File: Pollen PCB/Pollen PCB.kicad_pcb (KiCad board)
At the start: 2 copper layers, 3 parts, among them U1 DS18B20, U2 Pico

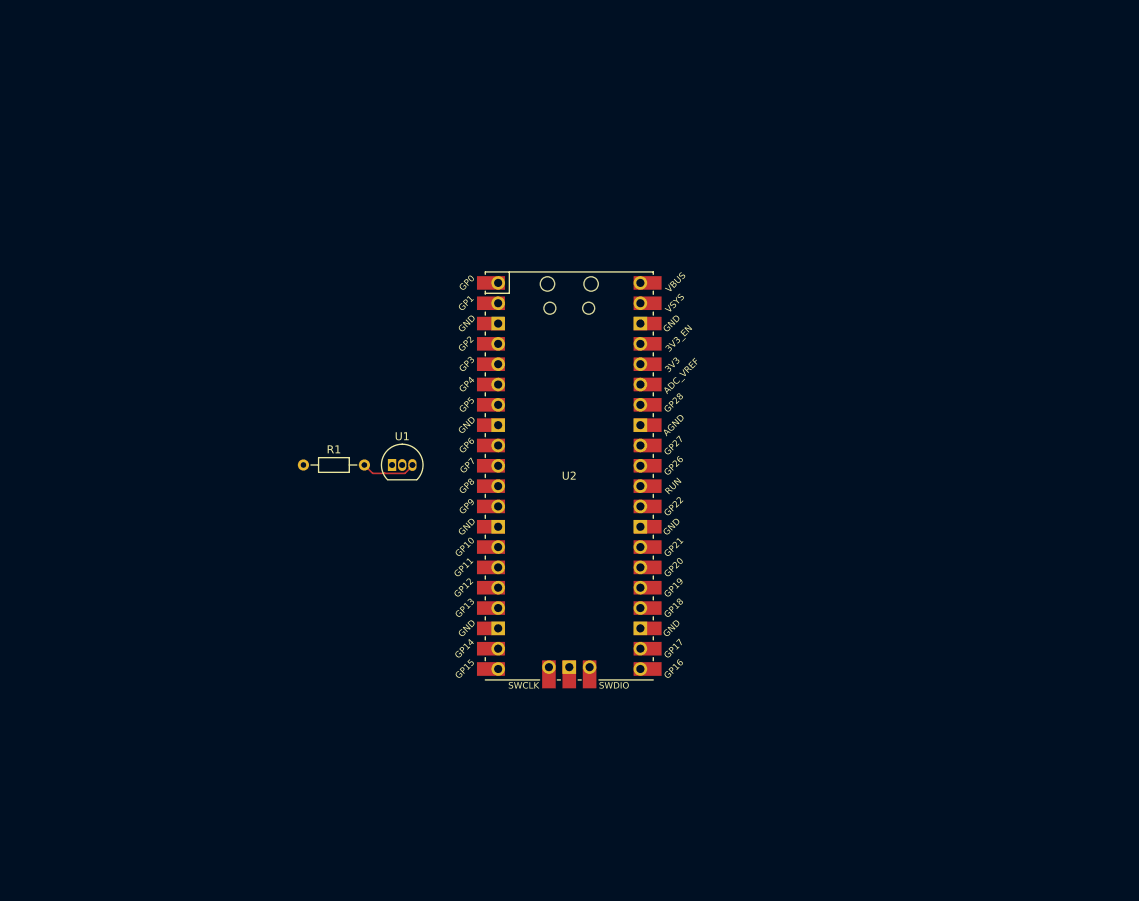
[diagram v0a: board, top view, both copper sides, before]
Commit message: Start drawing the schematic
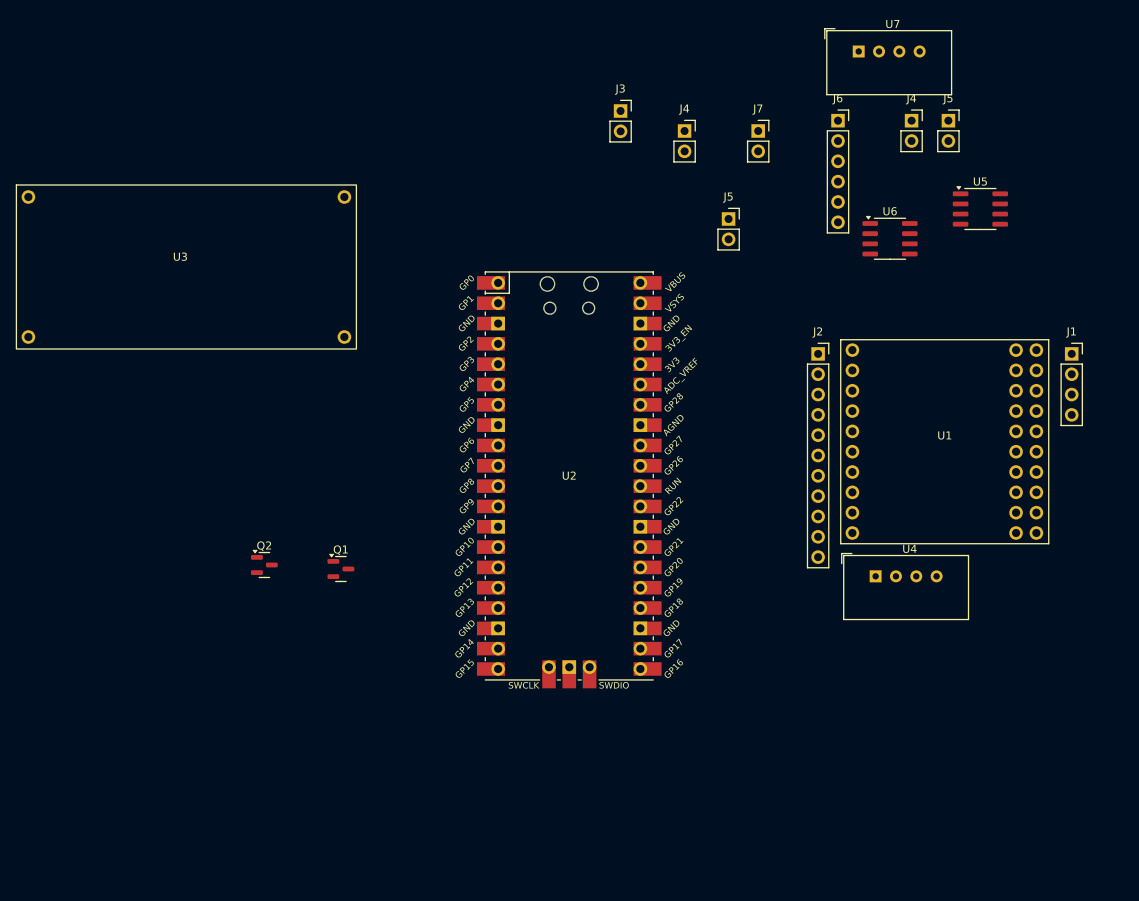
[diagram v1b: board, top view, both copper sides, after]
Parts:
- removed R1: R, Resistor_THT:R_Axial_DIN0204_L3.6mm_D1.6mm_P7.62mm_Horizontal
- added J1: GY-GPS6MV2, Connector_PinSocket_2.54mm:PinSocket_1x04_P2.54mm_Vertical, F.Cu at (228.4, 80.1)
- added J2: Conn_01x11_Socket, Connector_PinSocket_2.54mm:PinSocket_1x11_P2.54mm_Vertical, F.Cu at (196.7, 80.1)
- added J3: Solar_panel, Connector_PinSocket_2.54mm:PinSocket_1x02_P2.54mm_Vertical, F.Cu at (172.0, 49.8)
- added J4: Solar_panel, Connector_PinSocket_2.54mm:PinSocket_1x02_P2.54mm_Vertical, F.Cu at (180.0, 52.2)
- added J4: Solar_panel, Connector_PinSocket_2.54mm:PinSocket_1x02_P2.54mm_Vertical, F.Cu at (208.4, 51.0)
- added J5: Solar_charger, Connector_PinSocket_2.54mm:PinSocket_1x02_P2.54mm_Vertical, F.Cu at (185.5, 63.2)
- added J5: Solar_charger, Connector_PinSocket_2.54mm:PinSocket_1x02_P2.54mm_Vertical, F.Cu at (213.0, 51.0)
- added J6: Raspberry Pi, Connector_PinSocket_2.54mm:PinSocket_1x06_P2.54mm_Vertical, F.Cu at (199.2, 51.0)
- added J7: Battery, Connector_PinSocket_2.54mm:PinSocket_1x02_P2.54mm_Vertical, F.Cu at (189.2, 52.2)
- added Q1: Si2319CDS, Package_TO_SOT_SMD:SOT-23, F.Cu at (137.1, 107.0)
- added Q2: MMBT2222A, Package_TO_SOT_SMD:SOT-23, F.Cu at (127.5, 106.5)
- added U3: XL6009_DC-DC, Custom_Components:XL6009_DC-DC, F.Cu at (117.0, 68.5)
- added U4: DHT22, Sensor:ASAIR_AM2302_P2.54mm_Vertical, F.Cu at (203.9, 107.9)
- added U5: INA219AxD, Package_SO:SOIC-8_3.9x4.9mm_P1.27mm, F.Cu at (217.0, 62.0)
- added U6: INA219AxD, Package_SO:SOIC-8_3.9x4.9mm_P1.27mm, F.Cu at (205.7, 65.7)
- added U7: DHT22, Sensor:ASAIR_AM2302_P2.54mm_Vertical, F.Cu at (201.8, 42.3)
- U1: value DS18B20 -> NB-IOT-BC660; footprint Package_TO_SOT_THT:TO-92_Inline -> Custom_Components:NB-IOT-BC660
- moved U1 69.2 mm to (212.5, 90.8)
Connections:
- U1 pad 2: Net-(U1-DQ) -> unconnected-(U1-Pin_2-Pad2)
- U1 pad 3: Net-(U1-V_{DD}) -> unconnected-(U1-VCC-Pad3)
- U2 pad 4: unconnected-(U2-GPIO2-Pad4) -> Net-(U2-GPIO2)
- U2 pad 6: unconnected-(U2-GPIO4-Pad6) -> Net-(U2-GPIO4)
- U2 pad 7: unconnected-(U2-GPIO5-Pad7) -> Net-(U2-GPIO5)
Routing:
- net Net-(U1-V_{DD}): track 6.98 -> 0.00 mm

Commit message: Schematic v1.0
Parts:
- added C1: 100nF, Capacitor_THT:C_Axial_L5.1mm_D3.1mm_P10.00mm_Horizontal, F.Cu at (224.0, 116.5)
- added Q3: MMBT2222A, Package_TO_SOT_SMD:SOT-23, F.Cu at (129.6, 118.9)
- added Q4: Si2319CDS, Package_TO_SOT_SMD:SOT-23, F.Cu at (129.6, 123.5)
- J2: value Conn_01x11_Socket -> Adafruit Charge Controller
- moved U4 12.2 mm to (204.2, 120.1)
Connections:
- net BATT_CHG renamed /CHARGER_LIPO
- net BATT_V+ renamed /BATTERY+
- net Net-(U2-GPIO2) renamed /3V3_SENSOR_CONTROL
- net Net-(U2-GPIO4) renamed /SDA
- net Net-(U2-GPIO5) renamed /SCL
- net SOLAR_CHG renamed /CHARGER_V+
- net SOLAR_V+ renamed /SOLAR_V+
- J1 pad 1: unconnected-(J1-VCC-Pad1) -> +5V
- J1 pad 2: unconnected-(J1-RX-Pad2) -> /GPS_RX
- J1 pad 3: unconnected-(J1-TX-Pad3) -> /GPS_TX
- J1 pad 4: unconnected-(J1-GND-Pad4) -> GND
- J2 pad 11: unconnected-(J2-GND-Pad11) -> GND
- J2 pad 6: unconnected-(J2-PGOOD-Pad6) -> /CHARGER_PGOOD
- J2 pad 7: unconnected-(J2-CHG-Pad7) -> /CHARGER_CHG
- J2 pad 8: VCC -> +BATT
- J2 pad 9: unconnected-(J2-GND-Pad9) -> GND
- J6 pad 1: VCC_5V -> +5V
- J6 pad 3: unconnected-(J6-Pin_3-Pad3) -> /RPI_MOSI
- J6 pad 4: unconnected-(J6-Pin_4-Pad4) -> /RPI_MISO
- J6 pad 5: unconnected-(J6-Pin_5-Pad5) -> /RPI_SCK
- J6 pad 6: unconnected-(J6-Pin_6-Pad6) -> /RPI_CS
- Q1 pad 3: VCC -> +BATT
- U1 pad 19: unconnected-(U1-RxD-Pad19) -> /NB-IOT_RX
- U1 pad 20: unconnected-(U1-TxD-Pad20) -> /NB-IOT_TX
- U1 pad 3: unconnected-(U1-VCC-Pad3) -> +3V3
- U1 pad 4: unconnected-(U1-GND-Pad4) -> GND
- U1 pad 9: unconnected-(U1-RST-Pad9) -> /NB-IOT_RST
- U2 pad 1: unconnected-(U2-GPIO0-Pad1) -> /NB-IOT_RX
- U2 pad 11: unconnected-(U2-GPIO8-Pad11) -> /GPS_RX
- U2 pad 12: unconnected-(U2-GPIO9-Pad12) -> /GPS_TX
- U2 pad 13: unconnected-(U2-GND-Pad13) -> GND
- U2 pad 14: unconnected-(U2-GPIO10-Pad14) -> /CHARGER_CHG
- U2 pad 15: unconnected-(U2-GPIO11-Pad15) -> /CHARGER_PGOOD
- U2 pad 18: unconnected-(U2-GND-Pad18) -> GND
- U2 pad 19: unconnected-(U2-GPIO14-Pad19) -> /DHT_1
- U2 pad 2: unconnected-(U2-GPIO1-Pad2) -> /NB-IOT_TX
- U2 pad 20: unconnected-(U2-GPIO15-Pad20) -> /DHT_2
- U2 pad 21: unconnected-(U2-GPIO16-Pad21) -> /RPI_MISO
- U2 pad 22: unconnected-(U2-GPIO17-Pad22) -> /RPI_CS
- U2 pad 23: unconnected-(U2-GND-Pad23) -> GND
- U2 pad 24: unconnected-(U2-GPIO18-Pad24) -> /RPI_SCK
- U2 pad 25: unconnected-(U2-GPIO19-Pad25) -> /RPI_MOSI
- U2 pad 28: unconnected-(U2-GND-Pad28) -> GND
- U2 pad 3: unconnected-(U2-GND-Pad3) -> GND
- U2 pad 36: unconnected-(U2-3V3-Pad36) -> +3V3
- U2 pad 38: unconnected-(U2-GND-Pad38) -> GND
- U2 pad 39: unconnected-(U2-VSYS-Pad39) -> +BATT
- U2 pad 5: unconnected-(U2-GPIO3-Pad5) -> /5V_CONTROL
- U2 pad 8: unconnected-(U2-GND-Pad8) -> GND
- U2 pad 9: unconnected-(U2-GPIO6-Pad9) -> /NB-IOT_RST
- U3 pad 3: VCC_5V -> +5V
- U4 pad 1: unconnected-(U4-VDD-Pad1) -> +3V3_SENSOR
- U4 pad 2: unconnected-(U4-SDA-Pad2) -> /DHT_1
- U4 pad 3: Net-(U4-GND-Pad3) -> GND
- U4 pad 4: Net-(U4-GND-Pad3) -> GND
- U5 pad 1: unconnected-(U5-A1-Pad1) -> GND
- U5 pad 2: unconnected-(U5-A0-Pad2) -> GND
- U5 pad 5: VCC -> +3V3
- U6 pad 1: unconnected-(U6-A1-Pad1) -> GND
- U6 pad 2: unconnected-(U6-A0-Pad2) -> +3V3
- U6 pad 5: VCC -> +3V3
- U7 pad 1: unconnected-(U7-VDD-Pad1) -> +3V3_SENSOR
- U7 pad 2: unconnected-(U7-SDA-Pad2) -> /DHT_2
- U7 pad 3: Net-(U7-GND-Pad3) -> GND
- U7 pad 4: Net-(U7-GND-Pad3) -> GND

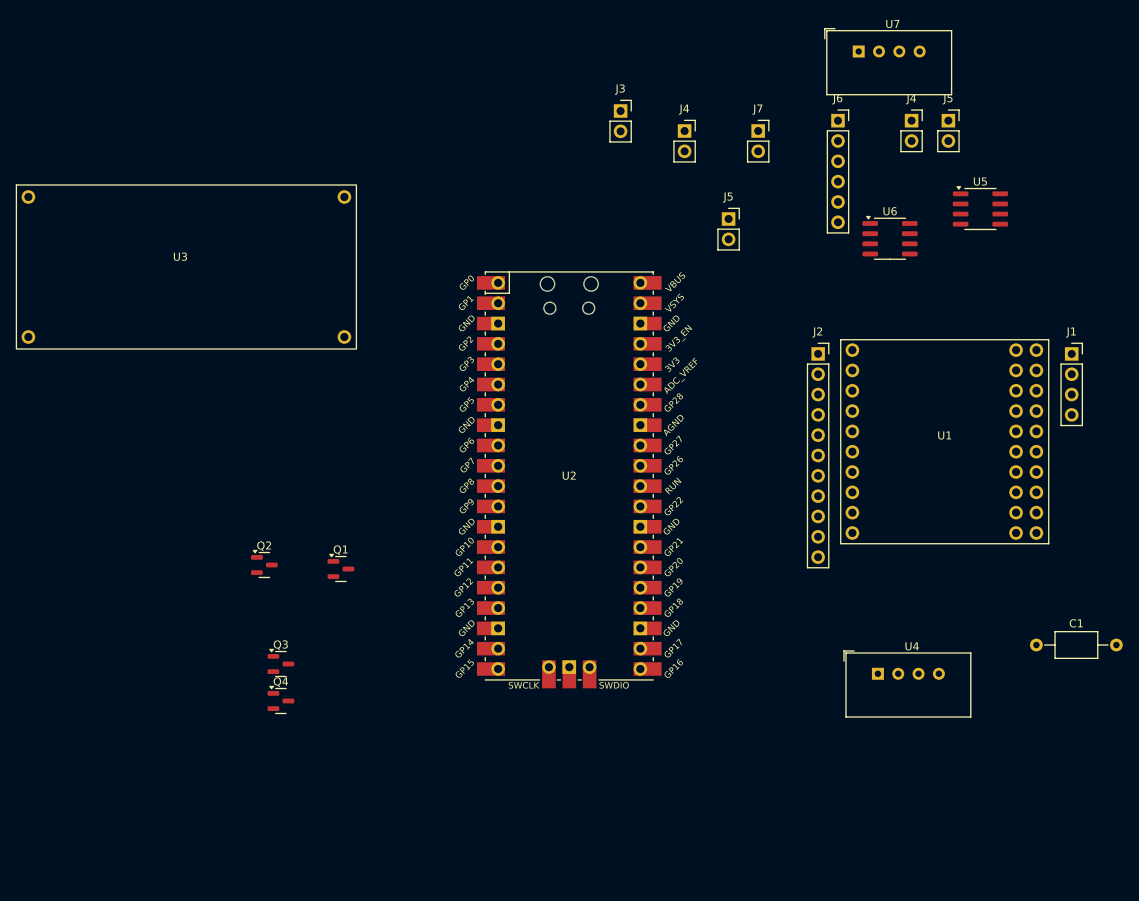
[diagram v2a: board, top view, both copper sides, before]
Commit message: PCB footprints organised
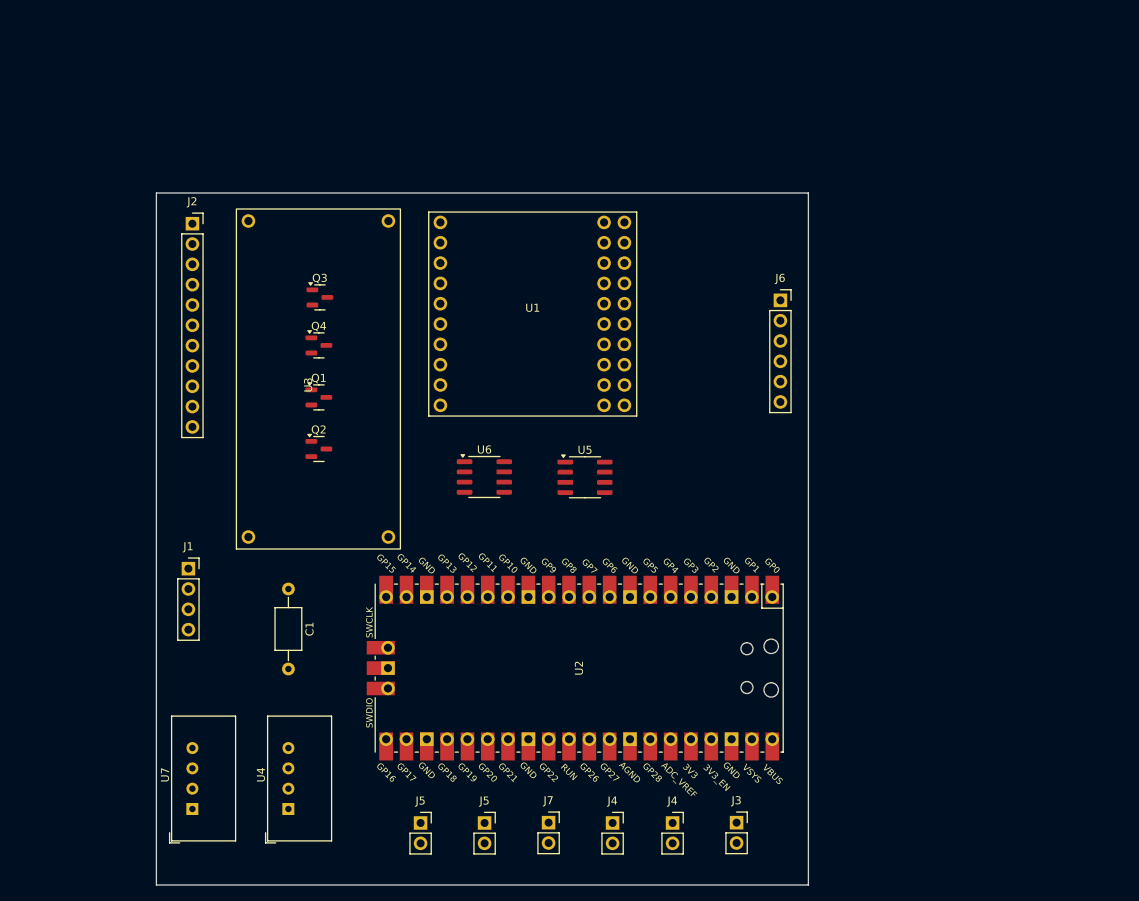
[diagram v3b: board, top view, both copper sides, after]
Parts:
- moved U7 126.1 mm to (118.5, 137.0), turned to 90 degrees
- moved J1 113.6 mm to (118.0, 107.0)
- moved J5 105.2 mm to (155.0, 138.8)
- moved J4 95.4 mm to (171.0, 138.8)
- moved C1 93.8 mm to (130.5, 109.5), turned to -90 degrees
- moved J7 90.3 mm to (163.0, 138.7)
- moved J3 90.1 mm to (186.5, 138.7)
- moved J4 86.5 mm to (178.5, 138.8)
- moved J5 84.7 mm to (147.0, 138.8)
- moved J2 79.9 mm to (118.5, 63.8)
- moved U4 75.6 mm to (130.5, 137.0), turned to 90 degrees
- moved U5 59.7 mm to (167.6, 95.5)
- moved U6 58.8 mm to (155.0, 95.5)
- moved U1 53.9 mm to (161.0, 74.9)
- moved Q3 46.1 mm to (134.4, 73.0)
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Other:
- board outline added: 81.5 x 86.5 mm

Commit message: Updated PCB + footprints
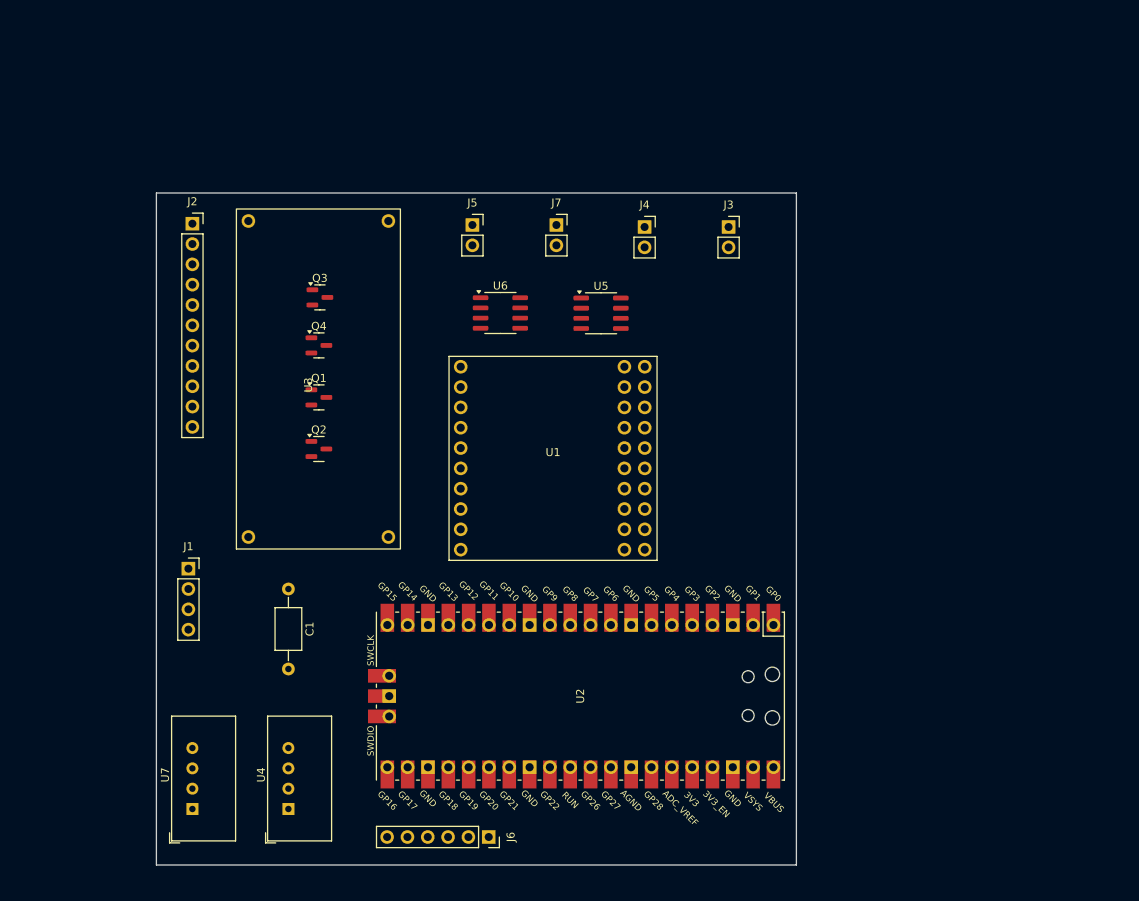
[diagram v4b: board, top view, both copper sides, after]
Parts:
- removed the J4 at (171.0, 138.8)
- removed the J5 at (155.0, 138.8)
- moved J6 76.3 mm to (155.5, 140.5), turned to -90 degrees
- moved J5 75.0 mm to (153.5, 64.0)
- moved J7 74.7 mm to (164.0, 64.0)
- moved J4 74.6 mm to (175.0, 64.2)
- moved J3 74.5 mm to (185.5, 64.2)
- moved U5 20.6 mm to (169.6, 75.0)
- moved U6 20.6 mm to (157.0, 75.0)
- moved U1 18.2 mm to (163.6, 92.9)
- moved U2 3.50 mm to (167.0, 122.9)
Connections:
- J6 pad 4: /RPI_MISO -> /RPI_SCK
- J6 pad 5: /RPI_SCK -> /RPI_CS
- J6 pad 6: /RPI_CS -> /RPI_MISO
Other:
- board size 81.5 x 86.5 mm -> 80 x 84 mm

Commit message: Update PCB
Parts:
- added J8: RPi power, Connector_PinSocket_2.54mm:PinSocket_1x02_P2.54mm_Vertical, F.Cu at (149.0, 100.3)
- added R1: 100m, Resistor_SMD:R_2512_6332Metric_Pad1.40x3.35mm_HandSolder, B.Cu at (136.0, 69.8)
- added R10: 10k, Resistor_SMD:R_1206_3216Metric_Pad1.30x1.75mm_HandSolder, B.Cu at (162.5, 102.3)
- added R2: 100m, Resistor_SMD:R_2512_6332Metric_Pad1.40x3.35mm_HandSolder, B.Cu at (125.8, 75.2)
- added R3: 10k, Resistor_SMD:R_1206_3216Metric_Pad1.30x1.75mm_HandSolder, B.Cu at (139.5, 84.5)
- added R4: 10k, Resistor_SMD:R_1206_3216Metric_Pad1.30x1.75mm_HandSolder, B.Cu at (142.0, 84.5)
- added R5: 10k, Resistor_SMD:R_1206_3216Metric_Pad1.30x1.75mm_HandSolder, B.Cu at (150.2, 64.8)
- added R6: 1k, Resistor_SMD:R_1206_3216Metric_Pad1.30x1.75mm_HandSolder, B.Cu at (149.0, 73.0)
- added R7: 1k, Resistor_SMD:R_1206_3216Metric_Pad1.30x1.75mm_HandSolder, B.Cu at (210.8, 102.2)
- added R8: 10k, Resistor_SMD:R_1206_3216Metric_Pad1.30x1.75mm_HandSolder, B.Cu at (203.7, 108.5)
- added R9: 5k1, Resistor_SMD:R_1206_3216Metric_Pad1.30x1.75mm_HandSolder, B.Cu at (165.0, 102.3)
- C1: footprint Capacitor_THT:C_Axial_L5.1mm_D3.1mm_P10.00mm_Horizontal -> Capacitor_SMD:C_1206_3216Metric_Pad1.33x1.80mm_HandSolder; moved to B.Cu
- J6: footprint Connector_PinSocket_2.54mm:PinSocket_1x06_P2.54mm_Vertical -> Connector_PinSocket_2.54mm:PinSocket_1x04_P2.54mm_Vertical
- Q1, Q2, Q3, Q4, U5, U6: moved to B.Cu
- moved Q4 78.0 mm to (206.7, 108.0), turned to -90 degrees
- moved Q3 77.7 mm to (205.7, 104.0), turned to -90 degrees
- moved J6 74.8 mm to (222.5, 107.2), turned to 0 degrees
- moved J1 52.9 mm to (170.1, 97.8), turned to -90 degrees
- moved U2 50.2 mm to (205.5, 90.8), turned to 0 degrees
- moved J3 44.5 mm to (141.0, 63.2)
- moved J4 38.0 mm to (137.0, 63.2)
- moved J7 35.0 mm to (129.0, 63.2)
- moved U5 32.3 mm to (137.2, 75.8), turned to 180 degrees
- moved J2 28.2 mm to (118.8, 92.0), turned to 180 degrees
- moved Q2 26.9 mm to (149.0, 69.5), turned to 90 degrees
- moved Q1 23.9 mm to (147.0, 65.2), turned to 90 degrees
- moved U6 23.6 mm to (135.0, 83.7), turned to -90 degrees
- moved C1 20.6 mm to (136.5, 89.8), turned to 180 degrees
- moved J5 20.5 mm to (133.0, 63.2)
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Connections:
- J1 pad 2: /GPS_RX -> unconnected-(J1-RX-Pad2)
- J1 pad 3: /GPS_TX -> Net-(J1-TX)
- J3 pad 1: /SOLAR_V+ -> GND
- J3 pad 2: GND -> /SOLAR_V+
- J4 pad 1: /SOLAR_V+ -> GND
- J4 pad 2: GND -> /SOLAR_V+
- J5 pad 1: /CHARGER_V+ -> GND
- J5 pad 2: GND -> /CHARGER_V+
- J6 pad 1: +5V -> /RPI_MOSI
- J6 pad 2: GND -> /RPI_SCK
- J6 pad 3: /RPI_MOSI -> /RPI_CS
- J6 pad 4: /RPI_SCK -> /RPI_MISO
- J7 pad 1: /BATTERY+ -> GND
- J7 pad 2: GND -> /BATTERY+
- U2 pad 11: /GPS_RX -> unconnected-(U2-GPIO8-Pad11)
- U2 pad 14: /CHARGER_CHG -> unconnected-(U2-GPIO10-Pad14)
- U2 pad 15: /CHARGER_PGOOD -> unconnected-(U2-GPIO11-Pad15)
- U2 pad 17: unconnected-(U2-GPIO13-Pad17) -> /DHT_1
- U2 pad 19: /DHT_1 -> unconnected-(U2-GPIO14-Pad19)
- U2 pad 26: unconnected-(U2-GPIO20-Pad26) -> /3V3_SENSOR_CONTROL
- U2 pad 27: unconnected-(U2-GPIO21-Pad27) -> /CHARGER_PGOOD
- U2 pad 29: unconnected-(U2-GPIO22-Pad29) -> /CHARGER_CHG
- U2 pad 4: /3V3_SENSOR_CONTROL -> /NB-IOT_RST
- U2 pad 9: /NB-IOT_RST -> unconnected-(U2-GPIO6-Pad9)
- U6 pad 7: /CHARGER_LIPO -> /BATTERY+
- U6 pad 8: /BATTERY+ -> /CHARGER_LIPO
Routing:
- net +3V3: track 0.00 -> 319.7 mm
- net /CHARGER_PGOOD: track 0.00 -> 172.5 mm
- net /CHARGER_CHG: track 0.00 -> 160.3 mm
- net +BATT: track 0.00 -> 126.9 mm
- net +3V3_SENSOR: track 0.00 -> 105.5 mm
- net /DHT_1: track 0.00 -> 91.1 mm
- net /SDA: track 0.00 -> 86.4 mm
- net /SCL: track 0.00 -> 77.0 mm
- net /5V_CONTROL: track 0.00 -> 73.0 mm
- net /DHT_2: track 0.00 -> 71.1 mm
- net /NB-IOT_TX: track 0.00 -> 61.6 mm
- net /NB-IOT_RST: track 0.00 -> 53.6 mm
- net GND: track 0.00 -> 53.3 mm, vias 0 -> 4
- net /NB-IOT_RX: track 0.00 -> 47.4 mm
- net +5V: track 0.00 -> 40.7 mm
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- added copper zone on B.Cu, net GND
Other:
- board size 80 x 84 mm -> 115.5 x 82.2 mm

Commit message: PCB first try
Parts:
- moved J3 2.38 mm to (139.0, 62.0)
- moved J4 2.38 mm to (135.0, 62.0)
- moved J5 2.38 mm to (131.0, 62.0)
- moved J7 2.38 mm to (127.0, 62.0)
- moved R6 0.25 mm to (148.8, 73.0)
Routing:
- net GND: track 53.3 -> 495.0 mm, vias 4 -> 0
- net +3V3: track 319.7 -> 317.6 mm
- net /CHARGER_V+: track 10.1 -> 12.2 mm
- net /SOLAR_V+: track 14.0 -> 16.0 mm
- net /BATTERY+: track 22.7 -> 24.8 mm
- removed copper zone on B.Cu, net GND
